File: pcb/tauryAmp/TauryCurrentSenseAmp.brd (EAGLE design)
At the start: 32.8 x 86.9 mm, 20 parts, among them IC1 AD780R, U1 MAX4239, U2 MAX4239

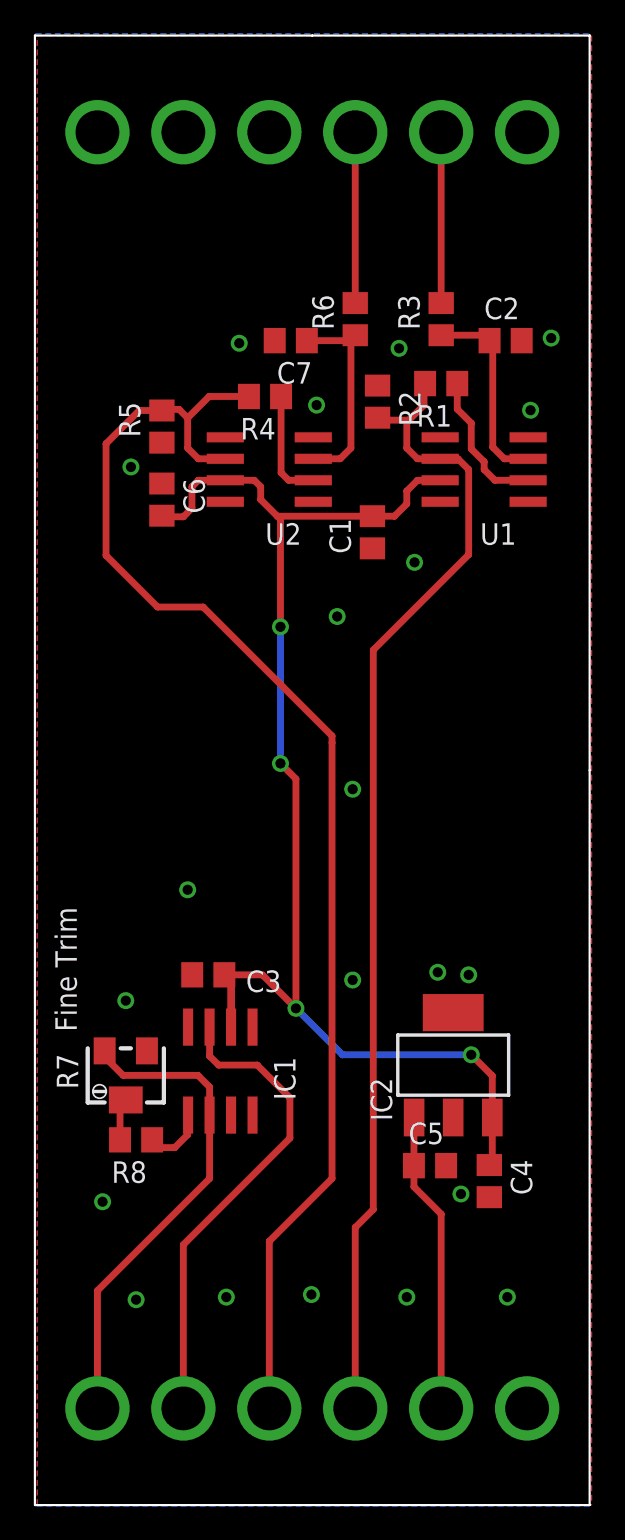
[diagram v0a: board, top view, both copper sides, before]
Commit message: improved analog frontend
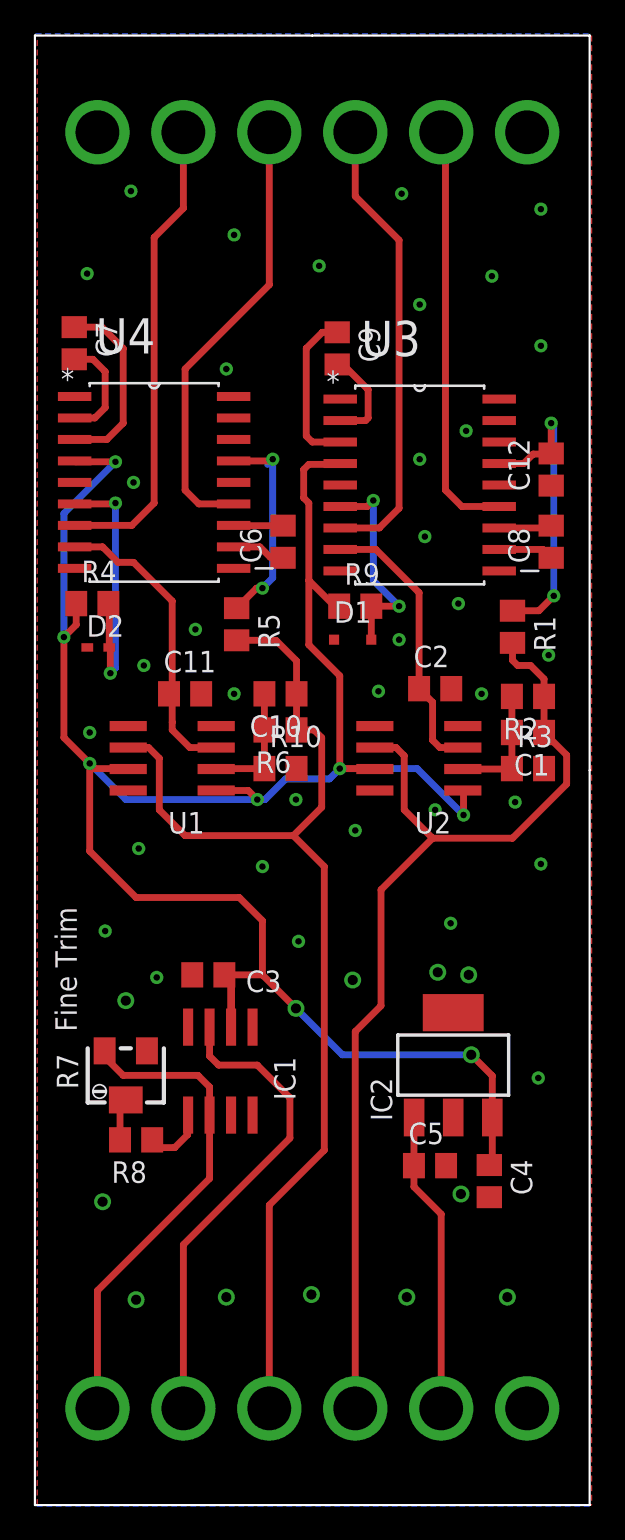
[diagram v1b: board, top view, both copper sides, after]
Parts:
- added C10, C11, C12: (no value), rcl:C0805
- added C8, C9: 1uF, rcl:C0805
- added D1: (no value), diode:SOD323-R
- added D2: (no value), diode:SOD523
- added R10: 1k, rcl:R0805
- added R9: 43k, rcl:R0805
- added U3, U4: LTC1043CSWPBF, LTC_By_element14_Batch_1:SOIC127P1032X264-18N
- C6, C7: value (none) -> 1uF
- R1: value 3.9k -> 10k
- R2, R6: value 100 -> 31.6k
- R3: value 100 -> 1k
- R4: value 3.9k -> 43k
- R5: value 100 -> 10k
- moved R3 27.1 mm to (29.3, 43.3), turned to 0 degrees
- moved U1 25.1 mm to (8.23, 43.9)
- moved R6 24.7 mm to (14.6, 45.6), turned to 180 degrees
- moved C2 21.0 mm to (23.8, 48.0)
- moved R2 19.6 mm to (29.3, 47.5), turned to 180 degrees
- moved U2 19.2 mm to (22.8, 43.9)
- moved R4 15.9 mm to (3.51, 53.0), turned to 0 degrees
- moved C1 15.0 mm to (29.3, 45.4), turned to 180 degrees
- moved R1 15.0 mm to (28.3, 51.7), turned to 270 degrees
- moved C7 12.8 mm to (2.44, 68.4), turned to 270 degrees
- moved R5 12.5 mm to (12.0, 51.8), turned to 270 degrees
- moved C6 7.58 mm to (14.8, 56.7), turned to 90 degrees
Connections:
- removed net N$12: U$1.10
- removed net N$13: U$1.11
- removed net SENSE1: R3.2, U$1.8
- removed net SENSE2: R6.2, U$1.9
- new net DDROP: D1.A, R9.2, U3.6
- new net DDROP2: D2.A, R4.2, U4.6
- new net IN1+: U$1.9, U3.7
- new net IN1-: U$1.8, U3.13
- new net IN2+: U$1.11, U4.7
- new net IN2-: U$1.10, U4.13
- new net N$10: C9.1, U3.3
- new net N$15: C6.2, U4.12
- new net N$16: C7.2, U4.2
- new net N$17: C7.1, U4.3
- new net N$18: C11.1, U1.3, U4.8
- new net N$19: R5.1, U4.15
- new net N$20: C10.2, R10.1, R6.2, U1.2
- new net N$7: C8.1, U3.11
- new net N$8: C8.2, U3.12
- new net N$9: C9.2, U3.2
- net GND: now also C11.2, C12.1, D1.C, D2.C, R10.2, R3.2, U3.14, U3.17, U3.18, U3.5, U4.14, U4.17, U4.18, U4.5; no longer C1.1, C6.1, C7.2, R2.1, R5.1
- net N$1: now also C2.1, U2.3, U3.8; no longer R4.1, U2.2
- net N$2: now also C12.2, U3.15; no longer U1.2
- net N$3: now also C6.1, U4.11; no longer C2.1, R3.1, U1.3
- net N$4: now also C1.2, R2.2, R3.1, U2.2; no longer C7.1, R6.1, U2.3
- net OUT1: now also C1.1, R2.1, U2.6; no longer R2.2, U1.6
- net OUT2: now also C10.1, R6.1, U1.6; no longer R4.2, U2.6
- net VCC: now also R4.1, R9.1, U1.1, U2.1, U3.4, U4.4; no longer C1.2, C6.2
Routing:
- net VCC: track 80.3 -> 131.5 mm, vias 4 -> 8
- net IN2+: track 0.00 -> 27.9 mm
- net IN1+: track 0.00 -> 27.3 mm
- net IN2-: track 0.00 -> 26.4 mm
- net IN1-: track 0.00 -> 24.8 mm
- net N$18: track 0.00 -> 18.0 mm
- net DDROP2: track 0.00 -> 16.8 mm, vias 0 -> 2
- net OUT2: track 80.0 -> 66.0 mm
- net N$19: track 0.00 -> 12.7 mm, vias 0 -> 2
- net DDROP: track 0.00 -> 12.6 mm, vias 0 -> 2
- net N$17: track 0.00 -> 11.1 mm
- net N$1: track 6.60 -> 16.7 mm
- net SENSE2: track 10.1 -> 0.00 mm
- net SENSE1: track 10.1 -> 0.00 mm
- net N$2: track 8.60 -> 18.3 mm, vias 0 -> 2
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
